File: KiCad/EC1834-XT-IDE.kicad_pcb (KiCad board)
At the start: 2 copper layers, 153.7 x 98.4 mm, 43 parts, among them J1 CONN_3, J2 CONN_3, J3 CONN_2, J4 CONN_2, J5 INTERRUPT, P6 CONN_1, P7 CONN_1, SW1 I/O ADDR, SW2 ROM OPT, U1 74LS573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

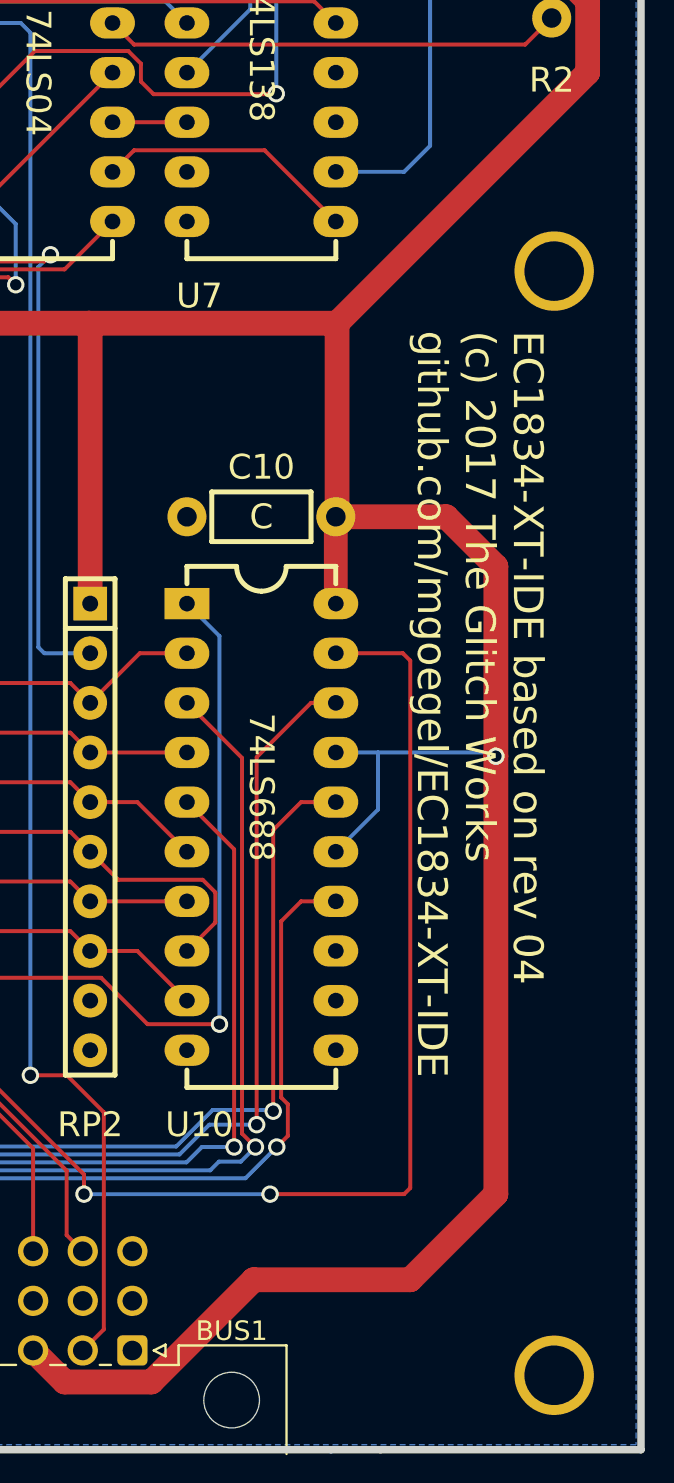
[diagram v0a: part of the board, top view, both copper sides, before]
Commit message: Added doc in German Added information about issues and how to solve
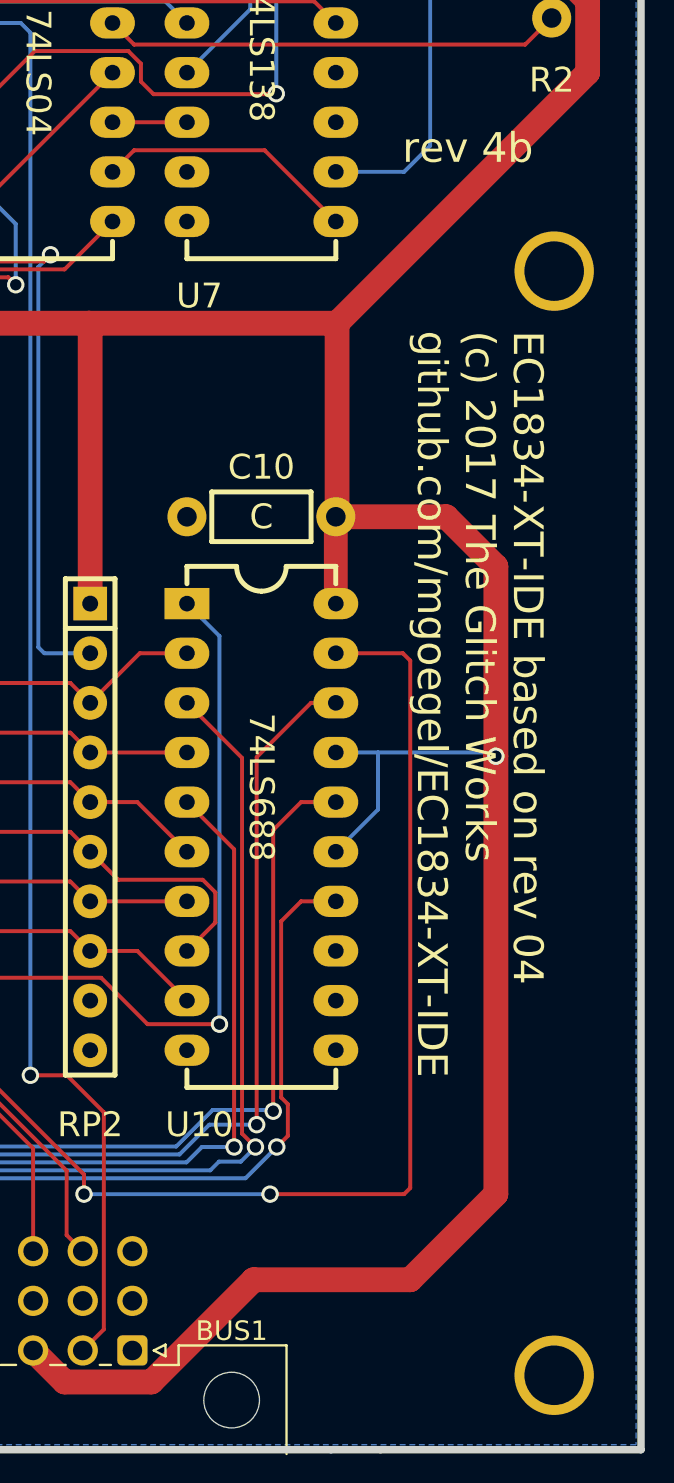
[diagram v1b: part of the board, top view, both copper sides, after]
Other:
- board text added: "rev 4b"

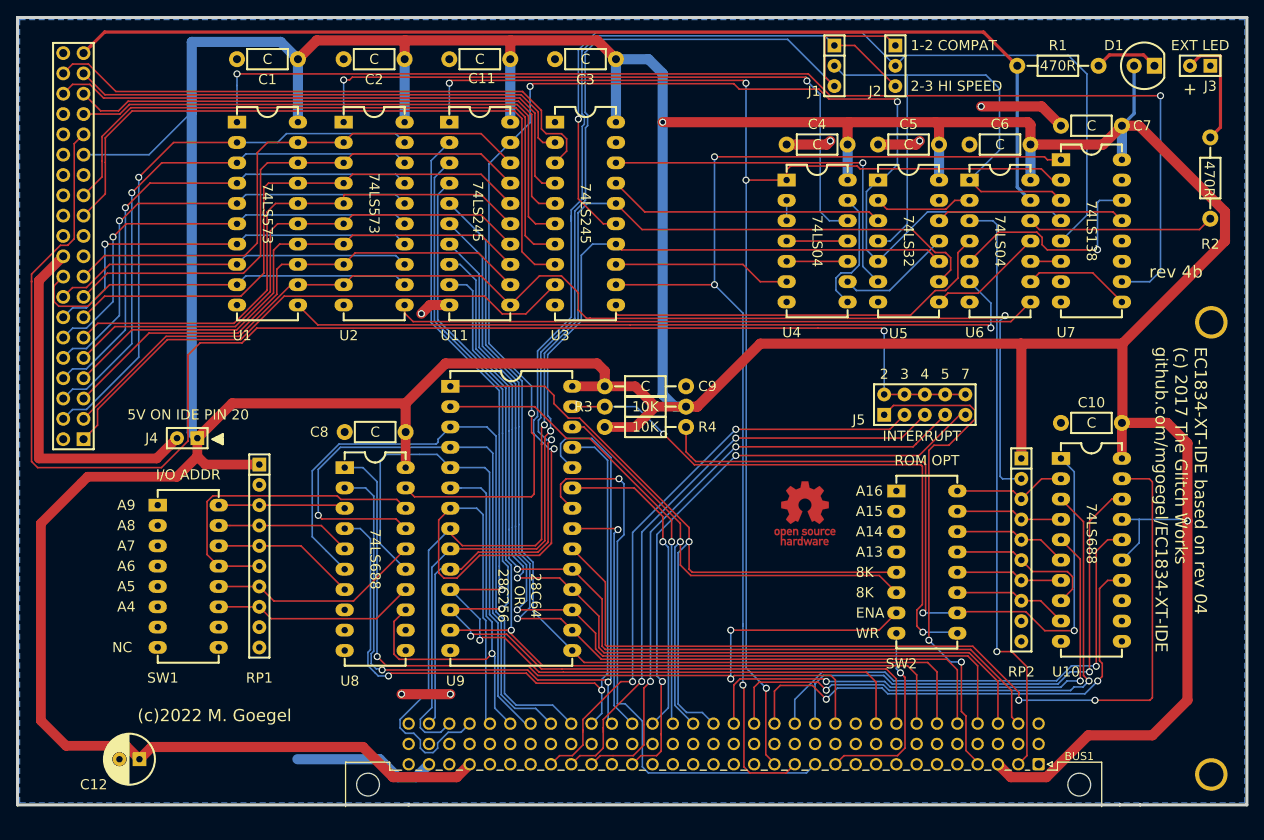
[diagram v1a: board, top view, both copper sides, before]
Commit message: Updated schema revision Updated gerber files Added default BIOS
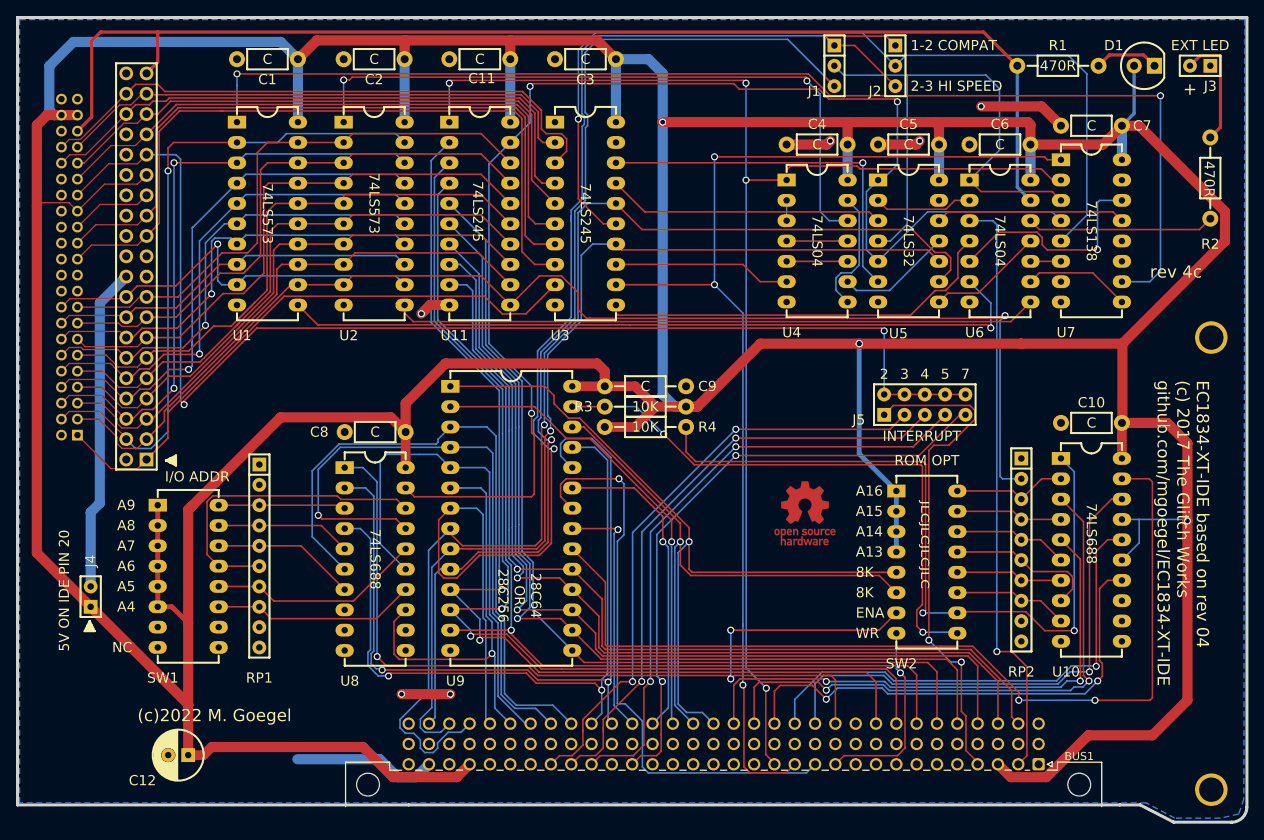
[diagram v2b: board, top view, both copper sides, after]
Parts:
- added IDE2: CONN_22X2, Connector_PinSocket_2.00mm:PinSocket_2x22_P2.00mm_Horizontal, B.Cu at (45.0, 97.9)
- added REF**: PIN1_TRIANGLE_SILKSCREEN, gw_symbols:PIN1_TRIANGLE_SILKSCREEN, B.Cu at (45.0, 99.9)
- added REF**: PIN1_TRIANGLE_SILKSCREEN, gw_symbols:PIN1_TRIANGLE_SILKSCREEN, F.Cu at (56.0, 101.1)
- moved REF** 27.4 mm to (46.5, 121.2), turned to 270 degrees
- moved J4 23.2 mm to (46.6, 118.1), turned to 180 degrees
- moved IDE1 8.27 mm to (53.6, 101.0)
- moved C12 6.12 mm to (58.8, 137.9)
- moved P6 1.91 mm to (186.7, 142.2)
- moved P7 1.91 mm to (186.7, 85.7)
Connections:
- RP1 pad 1: VCC -> GND
- RP2 pad 1: VCC -> GND
- SW1 pad 1: GND -> VCC
- SW1 pad 2: GND -> VCC
- SW1 pad 3: GND -> VCC
- SW1 pad 4: GND -> VCC
- SW1 pad 5: GND -> VCC
- SW1 pad 6: GND -> VCC
- SW2 pad 1: GND -> VCC
- SW2 pad 2: GND -> VCC
- SW2 pad 3: GND -> VCC
- SW2 pad 4: GND -> VCC
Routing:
- net VCC: track 714.5 -> 765.9 mm, vias 2 -> 4
- net /INTRQ: track 182.9 -> 156.1 mm, vias 1 -> 2
- net *DASP: track 137.1 -> 153.2 mm
- net /D8: track 71.1 -> 82.8 mm
- net /IORDY: track 0.00 -> 10.3 mm
- net /D9: track 66.9 -> 75.2 mm, vias 1 -> 2
- net D3: track 68.6 -> 75.2 mm
- net D7: track 152.4 -> 159.0 mm
- net /*IOW-IDE: track 86.1 -> 92.0 mm
- net /*IOR-IDE: track 82.2 -> 88.0 mm
- net /*RESET: track 69.9 -> 74.8 mm
- net /D10: track 62.6 -> 67.1 mm
- net D6: track 64.4 -> 68.8 mm
- net D5: track 65.4 -> 69.7 mm
- net /VCC_CF: track 44.9 -> 40.6 mm
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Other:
- board size 153.7 x 98.4 mm -> 153.7 x 100.6 mm
- board text added: "28C64 = 8K 8K SW ON 28C256 = 32K 8K SW OFF ENA = ON - BIOS ROM ENABLED WR = ON - BIOS WRITE ENABLE"
- board text added: "IO 2 2 2 2 3 3 3 3 0 4 8 C 0 4 8 C 0 0 0 0 0 0 0 0 A9 1 1 1 1 1 1 1 1 A8 0 0 0 0 1 1 1 1 A7 0 0 1 1 0 0 1 1 A6 0 1 0 1 0 1 0 1 A5 0 0 0 0 0 0 0 0 A4 0 0 0 0 0 0 0 0"
- board text added: "JLCJLCJLCJLC"
- board text added: "ROM ADDR 28C256 C D D 8 0 8 0 0 0 0 0 0 A16 0 1 1 A15 1 0 1 A14 0 0 0 A13 0 0 0"
- board text added: "rev 4c"
- board text removed: "28C64 = 8K 8K SW OFF 28C256 = 32K 8K SW ON ENA = OFF - BIOS ROM ENABLED! WR = OFF - BIOS WRITE ENABLE"
- board text removed: "IO 2 2 2 2 3 3 3 3 0 4 8 C 0 4 8 C 0 0 0 0 0 0 0 0 A9 0 0 0 0 0 0 0 0 A8 1 1 1 1 0 0 0 0 A7 1 1 0 0 1 1 0 0 A6 1 0 1 0 1 0 1 0 A5 1 1 1 1 1 1 1 1 A4 1 1 1 1 1 1 1 1"
- board text removed: "ROM ADDR 28C256 C D D 8 0 8 0 0 0 0 0 0 A16 1 0 0 A15 0 1 0 A14 1 1 1 A13 1 1 1"
- board text removed: "rev 4b"
